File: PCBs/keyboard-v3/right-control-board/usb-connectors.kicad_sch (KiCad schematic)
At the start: 12 parts, among them J101 USB4510-03-1-A, J102 USB4510-03-1-A, J103 GSB12J21C1EU, J201 USB4510-03-1-A, U104 USBLC6-4SC6, U201 USBLC6-4SC6

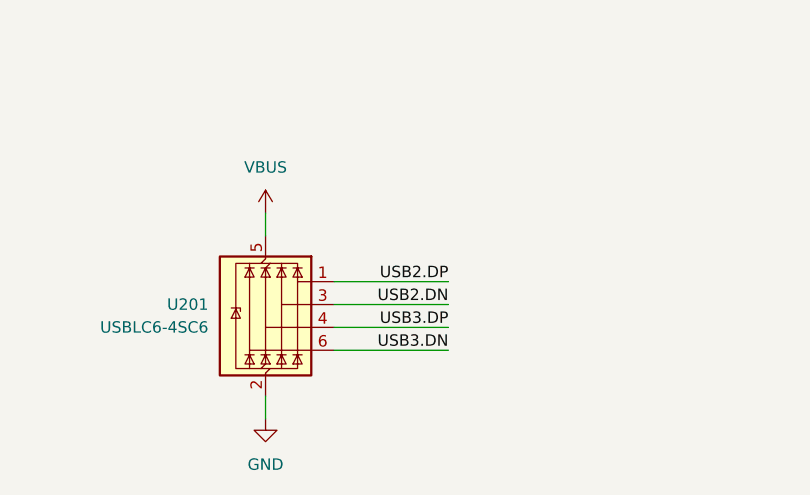
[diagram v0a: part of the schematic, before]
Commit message: Right control board placement and schematic done
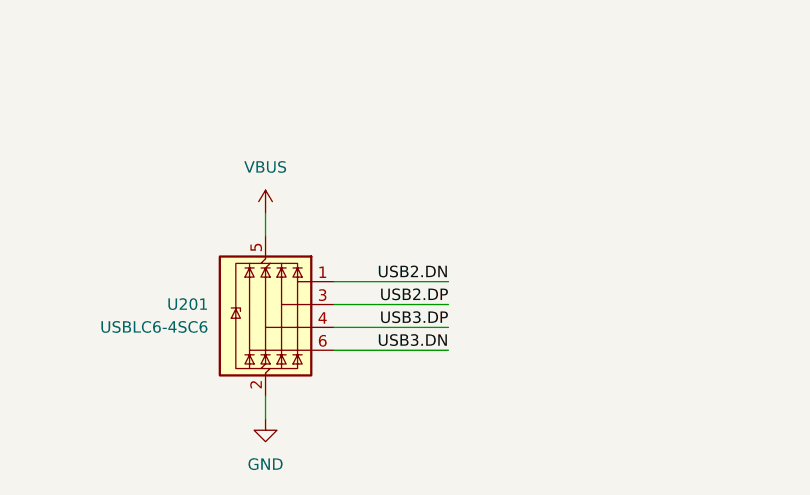
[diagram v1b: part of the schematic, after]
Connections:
- net USB2.DN: now also U201.1 (I/O1); no longer U201.3 (I/O2)
- net USB2.DP: now also U201.3 (I/O2); no longer U201.1 (I/O1)
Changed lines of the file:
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@@
 	)
 	(label "USB2.DP"
-		(at 226.06 129.54 180)
+		(at 226.06 132.08 180)
 		(effects
 			(font
@@
 	)
 	(label "USB2.DN"
-		(at 226.06 132.08 180)
+		(at 226.06 129.54 180)
 		(effects
 			(font

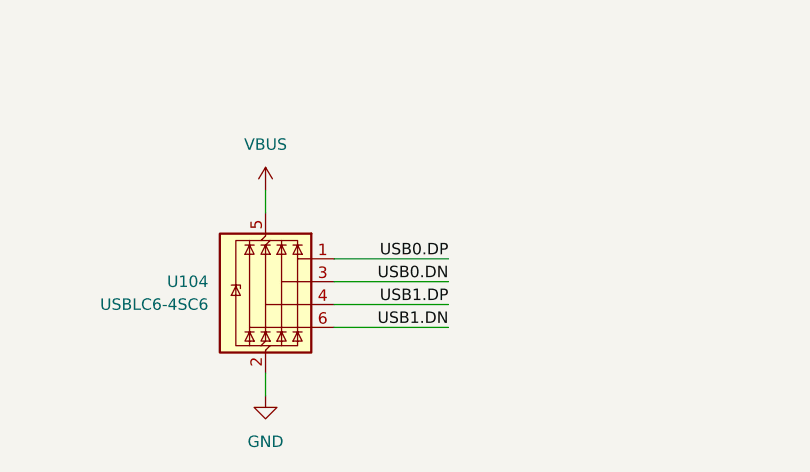
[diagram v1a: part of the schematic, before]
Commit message: Right control board ~50 unrouted
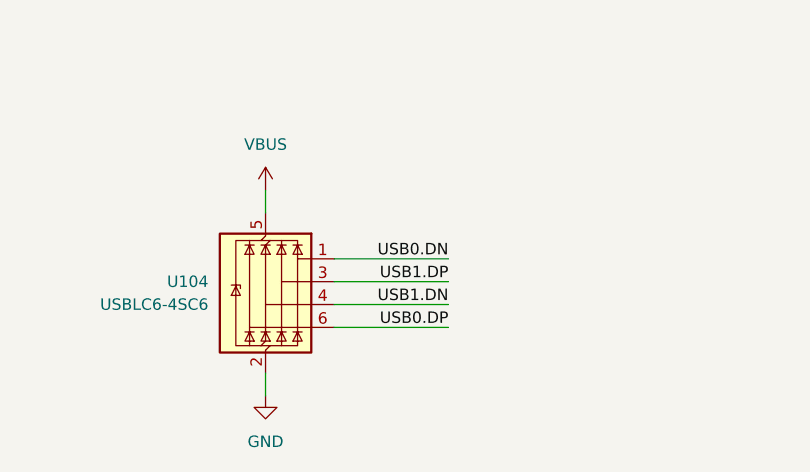
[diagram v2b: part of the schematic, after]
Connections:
- net USB0.DN: now also U104.1 (I/O1); no longer U104.3 (I/O2)
- net USB0.DP: now also U104.6 (I/O4); no longer U104.1 (I/O1)
- net USB1.DN: now also U104.4 (I/O3); no longer U104.6 (I/O4)
- net USB1.DP: now also U104.3 (I/O2); no longer U104.4 (I/O3)
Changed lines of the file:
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@@
 	)
 	(label "USB1.DP"
-		(at 144.78 134.62 180)
+		(at 144.78 132.08 180)
 		(effects
 			(font
@@
 	)
 	(label "USB0.DP"
-		(at 144.78 129.54 180)
+		(at 144.78 137.16 180)
 		(effects
 			(font
@@
 	)
 	(label "USB0.DN"
-		(at 144.78 132.08 180)
+		(at 144.78 129.54 180)
 		(effects
 			(font
@@
 	)
 	(label "USB1.DN"
-		(at 144.78 137.16 180)
+		(at 144.78 134.62 180)
 		(effects
 			(font

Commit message: Right control board routing finished
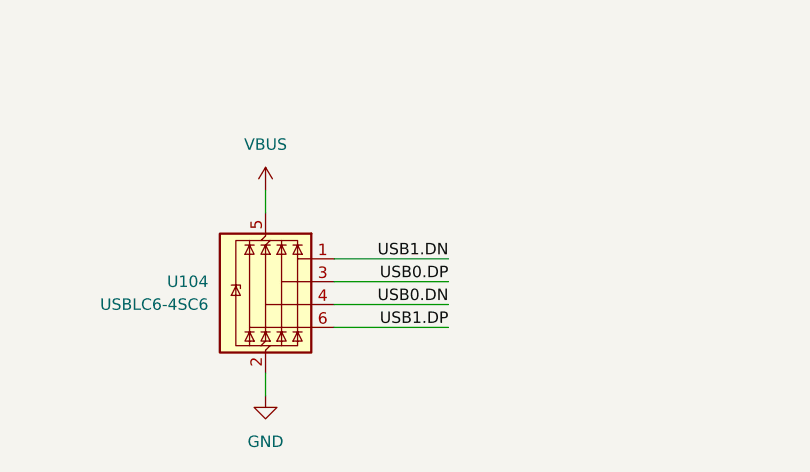
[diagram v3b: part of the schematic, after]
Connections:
- net USB0.DN: now also U104.4 (I/O3); no longer U104.1 (I/O1)
- net USB0.DP: now also U104.3 (I/O2); no longer U104.6 (I/O4)
- net USB1.DN: now also U104.1 (I/O1); no longer U104.4 (I/O3)
- net USB1.DP: now also U104.6 (I/O4); no longer U104.3 (I/O2)
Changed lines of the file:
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@@
 	)
 	(label "USB1.DP"
+		(at 144.78 137.16 180)
+		(effects
+			(font
+				(size 1.27 1.27)
+			)
+			(justify right bottom)
+		)
+	)
+	(label "USB0.DP"
 		(at 144.78 132.08 180)
 		(effects
@@
 		)
 	)
-	(label "USB0.DP"
-		(at 144.78 137.16 180)
-		(effects
-			(font
-				(size 1.27 1.27)
-			)
-			(justify right bottom)
-		)
-	)
 	(label "USB0.DN"
-		(at 144.78 129.54 180)
+		(at 144.78 134.62 180)
 		(effects
 			(font
@@
 	)
 	(label "USB1.DN"
-		(at 144.78 134.62 180)
+		(at 144.78 129.54 180)
 		(effects
 			(font

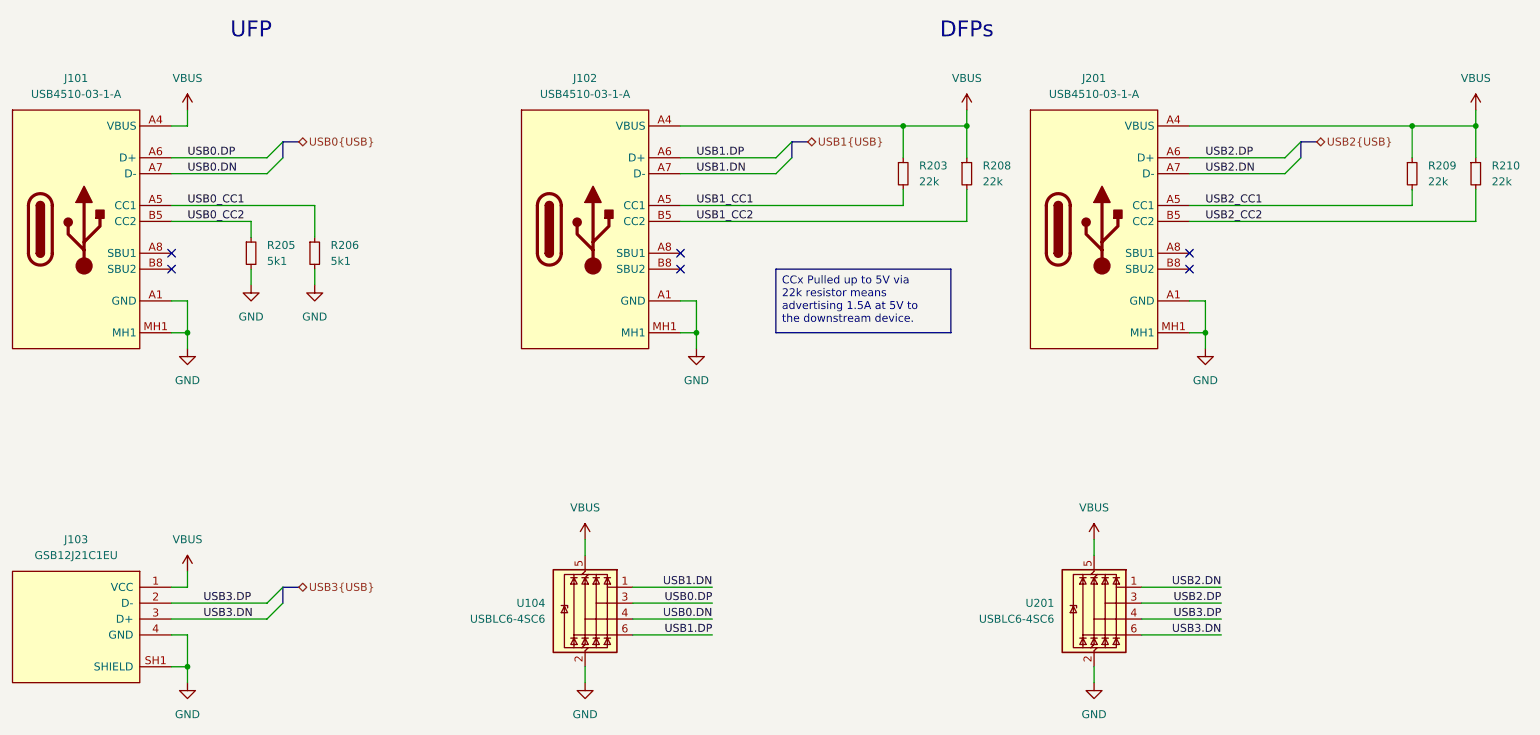
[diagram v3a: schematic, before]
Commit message: Added mounting holes
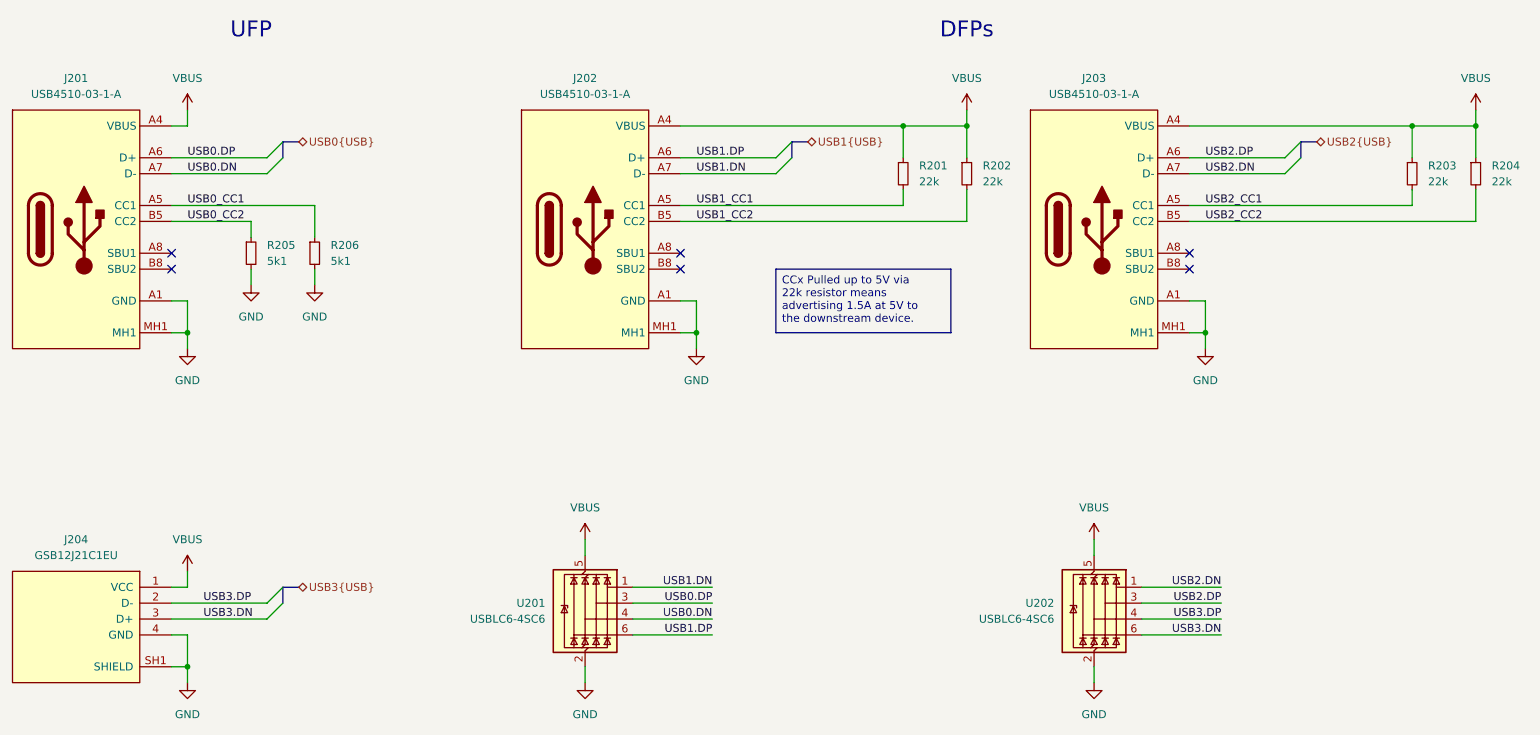
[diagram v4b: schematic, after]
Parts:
- renumbered J101 to J201, J102 to J202, J201 to J203, J103 to J204, R203 to R201, R208 to R202, R209 to R203, R210 to R204, U104 to U201, U201 to U202
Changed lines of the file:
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@@
 		(dnp no)
 		(fields_autoplaced yes)
-		(property "Reference" "J201"
+		(property "Reference" "J203"
 			(at 205.74 48.26 0)
 			(effects
@@
 			(project "right-control-board"
 				(path "/982f1c46-f6d6-42a2-bf2a-9fb0e913f11f/550affba-2d1b-4003-9291-dd582a27e02e"
-					(reference "J201")
+					(reference "J203")
 					(unit 1)
 				)
@@
 		(dnp no)
 		(fields_autoplaced yes)
-		(property "Reference" "#PWR0215"
+		(property "Reference" "#PWR0204"
 			(at 71.12 87.63 0)
 			(effects
@@
 			(project "right-control-board"
 				(path "/982f1c46-f6d6-42a2-bf2a-9fb0e913f11f/550affba-2d1b-4003-9291-dd582a27e02e"
-					(reference "#PWR0215")
+					(reference "#PWR0204")
 					(unit 1)
 				)
@@
 		(dnp no)
 		(fields_autoplaced yes)
-		(property "Reference" "J102"
+		(property "Reference" "J202"
 			(at 124.46 48.26 0)
 			(effects
@@
 			(project "right-control-board"
 				(path "/982f1c46-f6d6-42a2-bf2a-9fb0e913f11f/550affba-2d1b-4003-9291-dd582a27e02e"
-					(reference "J102")
+					(reference "J202")
 					(unit 1)
 				)
@@
 		(dnp no)
 		(fields_autoplaced yes)
-		(property "Reference" "#PWR0142"
+		(property "Reference" "#PWR0213"
 			(at 124.46 151.13 0)
 			(effects
@@
 			(project "right-control-board"
 				(path "/982f1c46-f6d6-42a2-bf2a-9fb0e913f11f/550affba-2d1b-4003-9291-dd582a27e02e"
-					(reference "#PWR0142")
+					(reference "#PWR0213")
 					(unit 1)
 				)
@@
 		(dnp no)
 		(fields_autoplaced yes)
-		(property "Reference" "U201"
+		(property "Reference" "U202"
 			(at 199.39 132.0799 0)
 			(effects
@@
 			(project "right-control-board"
 				(path "/982f1c46-f6d6-42a2-bf2a-9fb0e913f11f/550affba-2d1b-4003-9291-dd582a27e02e"
-					(reference "U201")
+					(reference "U202")
 					(unit 1)
 				)
@@
 		(dnp no)
 		(fields_autoplaced yes)
-		(property "Reference" "R209"
+		(property "Reference" "R203"
 			(at 259.08 62.2299 0)
 			(effects
@@
 			(project "right-control-board"
 				(path "/982f1c46-f6d6-42a2-bf2a-9fb0e913f11f/550affba-2d1b-4003-9291-dd582a27e02e"
-					(reference "R209")
+					(reference "R203")
 					(unit 1)
 				)
@@
 		(dnp no)
 		(fields_autoplaced yes)
-		(property "Reference" "R210"
+		(property "Reference" "R204"
 			(at 269.24 62.2299 0)
 			(effects
@@
 			(project "right-control-board"
 				(path "/982f1c46-f6d6-42a2-bf2a-9fb0e913f11f/550affba-2d1b-4003-9291-dd582a27e02e"
-					(reference "R210")
+					(reference "R204")
 					(unit 1)
 				)
@@
 		(dnp no)
 		(fields_autoplaced yes)
-		(property "Reference" "#PWR0204"
+		(property "Reference" "#PWR0212"
 			(at 60.96 151.13 0)
 			(effects
@@
 			(project "right-control-board"
 				(path "/982f1c46-f6d6-42a2-bf2a-9fb0e913f11f/550affba-2d1b-4003-9291-dd582a27e02e"
-					(reference "#PWR0204")
+					(reference "#PWR0212")
 					(unit 1)
 				)
@@
 		(dnp no)
 		(fields_autoplaced yes)
-		(property "Reference" "J103"
+		(property "Reference" "J204"
 			(at 43.18 121.92 0)
 			(effects
@@
 			(project "right-control-board"
 				(path "/982f1c46-f6d6-42a2-bf2a-9fb0e913f11f/550affba-2d1b-4003-9291-dd582a27e02e"
-					(reference "J103")
+					(reference "J204")
 					(unit 1)
 				)
@@
 		(dnp no)
 		(fields_autoplaced yes)
-		(property "Reference" "#PWR0216"
+		(property "Reference" "#PWR0205"
 			(at 81.28 87.63 0)
 			(effects
@@
 			(project "right-control-board"
 				(path "/982f1c46-f6d6-42a2-bf2a-9fb0e913f11f/550affba-2d1b-4003-9291-dd582a27e02e"
-					(reference "#PWR0216")
+					(reference "#PWR0205")
 					(unit 1)
 				)
@@
 		(dnp no)
 		(fields_autoplaced yes)
-		(property "Reference" "R203"
+		(property "Reference" "R201"
 			(at 177.8 62.2299 0)
 			(effects
@@
 			(project "right-control-board"
 				(path "/982f1c46-f6d6-42a2-bf2a-9fb0e913f11f/550affba-2d1b-4003-9291-dd582a27e02e"
-					(reference "R203")
+					(reference "R201")
 					(unit 1)
 				)
@@
 		(dnp no)
 		(fields_autoplaced yes)
-		(property "Reference" "#PWR0205"
+		(property "Reference" "#PWR0207"
 			(at 142.24 97.79 0)
 			(effects
@@
 			(project "right-control-board"
 				(path "/982f1c46-f6d6-42a2-bf2a-9fb0e913f11f/550affba-2d1b-4003-9291-dd582a27e02e"
-					(reference "#PWR0205")
+					(reference "#PWR0207")
 					(unit 1)
 				)
@@
 		(dnp no)
 		(fields_autoplaced yes)
-		(property "Reference" "#PWR0214"
+		(property "Reference" "#PWR0208"
 			(at 223.52 97.79 0)
 			(effects
@@
 			(project "right-control-board"
 				(path "/982f1c46-f6d6-42a2-bf2a-9fb0e913f11f/550affba-2d1b-4003-9291-dd582a27e02e"
-					(reference "#PWR0214")
+					(reference "#PWR0208")
 					(unit 1)
 				)
@@
 		(dnp no)
 		(fields_autoplaced yes)
-		(property "Reference" "#PWR0141"
+		(property "Reference" "#PWR0209"
 			(at 124.46 125.73 0)
 			(effects
@@
 			(project "right-control-board"
 				(path "/982f1c46-f6d6-42a2-bf2a-9fb0e913f11f/550affba-2d1b-4003-9291-dd582a27e02e"
-					(reference "#PWR0141")
+					(reference "#PWR0209")
 					(unit 1)
 				)
@@
 		(dnp no)
 		(fields_autoplaced yes)
-		(property "Reference" "R208"
+		(property "Reference" "R202"
 			(at 187.96 62.2299 0)
 			(effects
@@
 			(project "right-control-board"
 				(path "/982f1c46-f6d6-42a2-bf2a-9fb0e913f11f/550affba-2d1b-4003-9291-dd582a27e02e"
-					(reference "R208")
+					(reference "R202")
 					(unit 1)
 				)
@@
 		(dnp no)
 		(fields_autoplaced yes)
-		(property "Reference" "#PWR0209"
+		(property "Reference" "#PWR0210"
 			(at 205.74 125.73 0)
 			(effects
@@
 			(project "right-control-board"
 				(path "/982f1c46-f6d6-42a2-bf2a-9fb0e913f11f/550affba-2d1b-4003-9291-dd582a27e02e"
-					(reference "#PWR0209")
+					(reference "#PWR0210")
 					(unit 1)
 				)
@@
 		(dnp no)
 		(fields_autoplaced yes)
-		(property "Reference" "J101"
+		(property "Reference" "J201"
 			(at 43.18 48.26 0)
 			(effects
@@
 			(project "right-control-board"
 				(path "/982f1c46-f6d6-42a2-bf2a-9fb0e913f11f/550affba-2d1b-4003-9291-dd582a27e02e"
-					(reference "J101")
+					(reference "J201")
 					(unit 1)
 				)
@@
 		(dnp no)
 		(fields_autoplaced yes)
-		(property "Reference" "#PWR0210"
+		(property "Reference" "#PWR0214"
 			(at 205.74 151.13 0)
 			(effects
@@
 			(project "right-control-board"
 				(path "/982f1c46-f6d6-42a2-bf2a-9fb0e913f11f/550affba-2d1b-4003-9291-dd582a27e02e"
-					(reference "#PWR0210")
+					(reference "#PWR0214")
 					(unit 1)
 				)
@@
 		(dnp no)
 		(fields_autoplaced yes)
-		(property "Reference" "#PWR0203"
+		(property "Reference" "#PWR0211"
 			(at 60.96 130.81 0)
 			(effects
@@
 			(project "right-control-board"
 				(path "/982f1c46-f6d6-42a2-bf2a-9fb0e913f11f/550affba-2d1b-4003-9291-dd582a27e02e"
-					(reference "#PWR0203")
+					(reference "#PWR0211")
 					(unit 1)
 				)
@@
 		(dnp no)
 		(fields_autoplaced yes)
-		(property "Reference" "#PWR0212"
+		(property "Reference" "#PWR0203"
 			(at 266.7 57.15 0)
 			(effects
@@
 			(project "right-control-board"
 				(path "/982f1c46-f6d6-42a2-bf2a-9fb0e913f11f/550affba-2d1b-4003-9291-dd582a27e02e"
-					(reference "#PWR0212")
+					(reference "#PWR0203")
 					(unit 1)
 				)
@@
 		(dnp no)
 		(fields_autoplaced yes)
-		(property "Reference" "U104"
+		(property "Reference" "U201"
 			(at 118.11 132.0799 0)
 			(effects
@@
 			(project "right-control-board"
 				(path "/982f1c46-f6d6-42a2-bf2a-9fb0e913f11f/550affba-2d1b-4003-9291-dd582a27e02e"
-					(reference "U104")
+					(reference "U201")
 					(unit 1)
 				)
@@
 		(dnp no)
 		(fields_autoplaced yes)
-		(property "Reference" "#PWR0211"
+		(property "Reference" "#PWR0202"
 			(at 185.42 57.15 0)
 			(effects
@@
 			(project "right-control-board"
 				(path "/982f1c46-f6d6-42a2-bf2a-9fb0e913f11f/550affba-2d1b-4003-9291-dd582a27e02e"
-					(reference "#PWR0211")
-					(unit 1)
-				)
+					(reference "#PWR0202")
+					(unit 1)
+				)
